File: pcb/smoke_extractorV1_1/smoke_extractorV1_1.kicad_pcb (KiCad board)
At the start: 2 copper layers, 47 x 35 mm, 48 parts, among them J1 USB_C_Receptacle, J2 Screw_Terminal_01x02, Q1 AO3400A, U1 LMV331, U2 RA11131100, U3 MP1542, U4 LMV331, U5 LMV331, U6 STBP120

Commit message: More improvements in the pcb design
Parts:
- removed H4: MountingHole_Pad, MountingHole:MountingHole_3.2mm_M3_ISO7380_Pad
- moved R11 24.3 mm to (122.3, 121.5), turned to 180 degrees
- moved R19 23.1 mm to (123.4, 110.8), turned to 90 degrees
- moved C6 20.9 mm to (123.5, 118.5), turned to -90 degrees
- moved U4 20.7 mm to (126.2, 118.8), turned to 90 degrees
- moved C7 19.1 mm to (120.0, 108.2), turned to 180 degrees
- moved U5 17.8 mm to (119.6, 111.0), turned to 0 degrees
- moved R1 16.0 mm to (100.2, 116.8)
- moved R2 16.0 mm to (100.2, 120.5)
- moved R18 15.4 mm to (124.5, 114.8), turned to 180 degrees
- moved R13 13.3 mm to (115.9, 109.0), turned to -90 degrees
- moved Q1 12.2 mm to (116.5, 103.3), turned to -90 degrees
- moved C1 11.8 mm to (118.0, 116.0)
- moved R5 11.8 mm to (113.8, 117.2)
- moved R6 11.8 mm to (121.2, 118.5)
- moved U1 11.8 mm to (117.5, 118.8)
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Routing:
- net VBUS_RAW: track 4.79 -> 53.2 mm
- net V_CC_REF: track 0.00 -> 39.6 mm, vias 0 -> 3
- net CC1: track 0.00 -> 22.2 mm
- net CHG_DET: track 0.00 -> 18.1 mm, vias 0 -> 2
- net CC2: track 0.00 -> 17.5 mm, vias 0 -> 2
- net D-: track 3.20 -> 19.4 mm, vias 0 -> 2
- net CC2_DET: track 0.00 -> 13.2 mm, vias 0 -> 4
- net CC1_DET: track 0.00 -> 12.8 mm
- net D+: track 2.60 -> 13.9 mm
- net Net-(C8-Pad1): track 6.38 -> 12.0 mm
- net VDAT_REF: track 0.00 -> 4.44 mm
- net Net-(C4-Pad1): track 3.36 -> 0.41 mm
- net Net-(C4-Pad2): track 1.98 -> 0.00 mm
- added copper zone on F.Cu, net GND
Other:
- board size 47 x 35 mm -> 54 x 27 mm
- board text removed: "CHANGE THE USB C FOOTPRINT AND USE THE SWITCH W/ A SCREW TERMINAL"

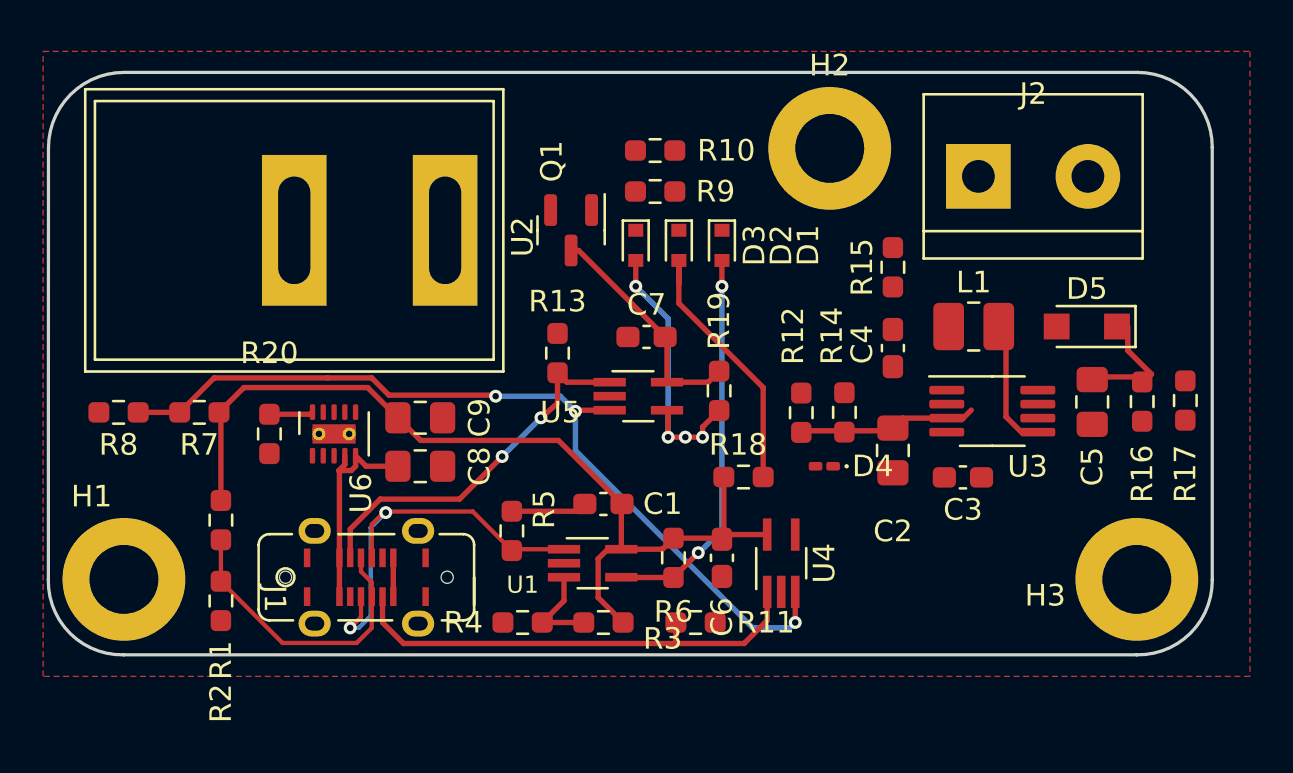
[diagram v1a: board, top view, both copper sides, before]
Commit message: Removed the voltage IC and one mounting hole. Missing boost converter conns only.
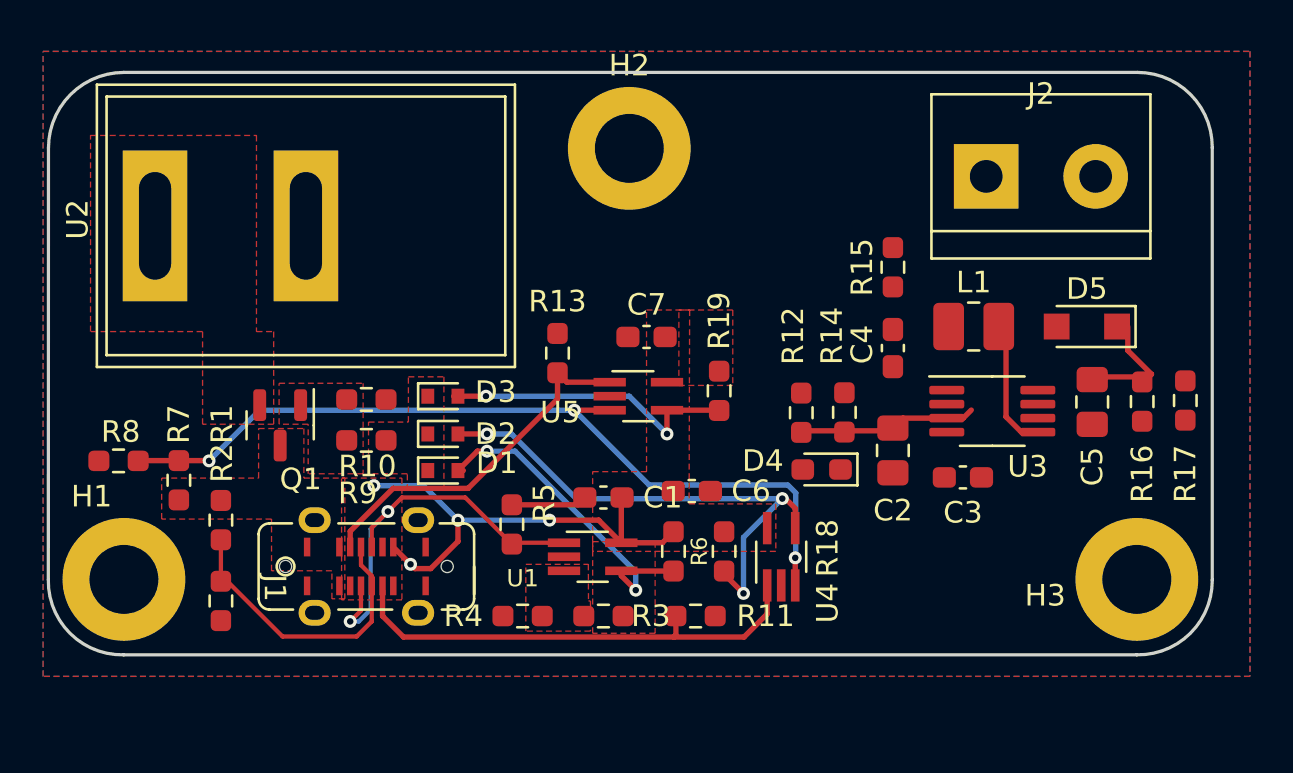
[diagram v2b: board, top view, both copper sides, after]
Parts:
- removed C8, C9: 10u, Capacitor_SMD:C_0805_2012Metric_Pad1.18x1.45mm_HandSolder
- removed R20: 100k, Resistor_SMD:R_0603_1608Metric_Pad0.98x0.95mm_HandSolder
- removed U6: STBP120, Package_DFN_QFN:TDFN-10-1EP_2x3mm_P0.5mm_EP0.9x2mm_ThermalVias
- D4: footprint LED_SMD:LED_0201_0603Metric_Pad0.64x0.40mm_HandSolder -> LED_SMD:LED_0603_1608Metric_Pad1.05x0.95mm_HandSolder
- moved U2 23.1 mm to (94.5, 96.5), turned to -90 degrees
- moved R10 17.7 mm to (107.0, 111.2)
- moved R9 17.7 mm to (107.0, 113.0)
- moved D1 16.6 mm to (110.5, 114.5), turned to 0 degrees
- moved Q1 16.3 mm to (103.0, 112.3)
- moved D2 14.0 mm to (110.5, 112.8), turned to 0 degrees
- moved D3 11.4 mm to (110.5, 111.0), turned to 0 degrees
- moved H2 9.30 mm to (119.2, 99.5)
- moved R18 3.57 mm to (123.6, 118.2), turned to 90 degrees
- moved C6 3.40 mm to (122.1, 115.4), turned to 0 degrees
- moved R7 3.29 mm to (98.3, 114.9), turned to -90 degrees
- moved R8 2.25 mm to (95.5, 114.0)
- moved J1 0.50 mm to (107.0, 118.9)
- moved J2 0.36 mm to (135.8, 100.8)
- moved C1 0.30 mm to (118.0, 115.7)
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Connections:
- J1 pad A4: Net-(C8-Pad1) -> VBUS_RAW
- J1 pad A9: Net-(C8-Pad1) -> VBUS_RAW
- J1 pad B4: Net-(C8-Pad1) -> VBUS_RAW
- J1 pad B9: Net-(C8-Pad1) -> VBUS_RAW
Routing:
- net VBUS_RAW: track 53.2 -> 23.0 mm, vias 0 -> 4
- net CC1_DET: track 12.8 -> 25.2 mm, vias 0 -> 3
- net Net-(C8-Pad1): track 12.0 -> 0.00 mm
- net VDAT_REF: track 4.44 -> 0.00 mm
- net CHG_DET: track 18.1 -> 15.7 mm
- net Net-(R20-Pad1): track 2.04 -> 0.00 mm
- net CC2_DET: track 13.2 -> 14.2 mm, vias 4 -> 2
- net CC2: track 17.5 -> 16.7 mm, vias 2 -> 0
- net V_CC_REF: track 39.6 -> 39.0 mm
- added copper zone on B.Cu, net GND
- added copper zone on F.Cu, net Net-(D1-Pad1)
- added copper zone on F.Cu, net Net-(Q1-Pad1)
- added copper zone on F.Cu, net VBUS_OPEN
- added copper zone on F.Cu, net VBUS_RAW
- added copper zone on F.Cu, net VDAT_REF

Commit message: Ready to place the order.
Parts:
- moved H2 23.5 mm to (142.8, 99.5)
- moved C4 15.1 mm to (119.5, 99.5), turned to 180 degrees
- moved R17 15.0 mm to (131.1, 105.7), turned to 180 degrees
- moved R12 14.7 mm to (115.8, 102.3)
- moved R14 14.7 mm to (117.8, 102.3), turned to -90 degrees
- moved D5 14.6 mm to (129.1, 98.6)
- moved L1 14.6 mm to (123.8, 98.6)
- moved U3 14.6 mm to (124.7, 102.5)
- moved C2 14.6 mm to (120.1, 104.4)
- moved C3 14.6 mm to (123.3, 105.6)
- moved D4 14.4 mm to (116.8, 105.5)
- moved R15 14.2 mm to (119.5, 97.4), turned to 0 degrees
- moved R16 14.1 mm to (132.2, 102.1)
- moved C5 14.1 mm to (130.0, 102.1)
- moved J2 8.42 mm to (141.5, 107.0), turned to -90 degrees
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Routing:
- net Net-(R16-Pad2): track 0.00 -> 18.7 mm, vias 0 -> 2
- net Net-(C3-Pad1): track 0.00 -> 7.60 mm, vias 0 -> 2
- net VBUS_SWITCH: track 8.29 -> 0.83 mm
- net Net-(D5-Pad2): track 5.80 -> 0.00 mm
- net VBOOST_OUT: track 4.97 -> 0.00 mm
- net GND: track 3.53 -> 0.00 mm, vias 0 -> 1
- net Net-(C4-Pad1): track 0.41 -> 3.81 mm
- net Net-(D4-Pad2): track 0.00 -> 2.29 mm
- net Net-(C4-Pad2): track 0.00 -> 2.12 mm
- net V_CC_REF: track 39.0 -> 40.9 mm
- net CC2: track 16.7 -> 15.5 mm
- net CC1_DET: track 25.2 -> 24.5 mm
- net VBUS_RAW: track 23.0 -> 22.4 mm
- net CC2_DET: track 14.2 -> 14.8 mm
- added copper zone on F.Cu, net Net-(D5-Pad2)
- added copper zone on F.Cu, net VBOOST_OUT
- added copper zone on F.Cu, net VBUS_SWITCH
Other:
- board text added: "5V@600mA 12V@200mA"
- board text added: "Nuno Nogueira Stockholm July 2022"
- board text added: "Smoke Extractor 1v1"

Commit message: Error checks.
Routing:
- net VBUS_RAW: track 22.4 -> 28.3 mm, vias 4 -> 3
- net VBUS_SWITCH: track 0.83 -> 0.00 mm
- net CC1_DET: track 24.5 -> 23.9 mm
- net GND: vias 1 -> 162
